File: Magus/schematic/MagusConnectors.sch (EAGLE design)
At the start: 48 parts, among them IC3 RC4560, J1 POWER_JACK, U1 REG_S9V11F5, U2 REG_U3V12F12, U3 ICL7660, X2 1503_09, X4 1503_09, X5 1503_09

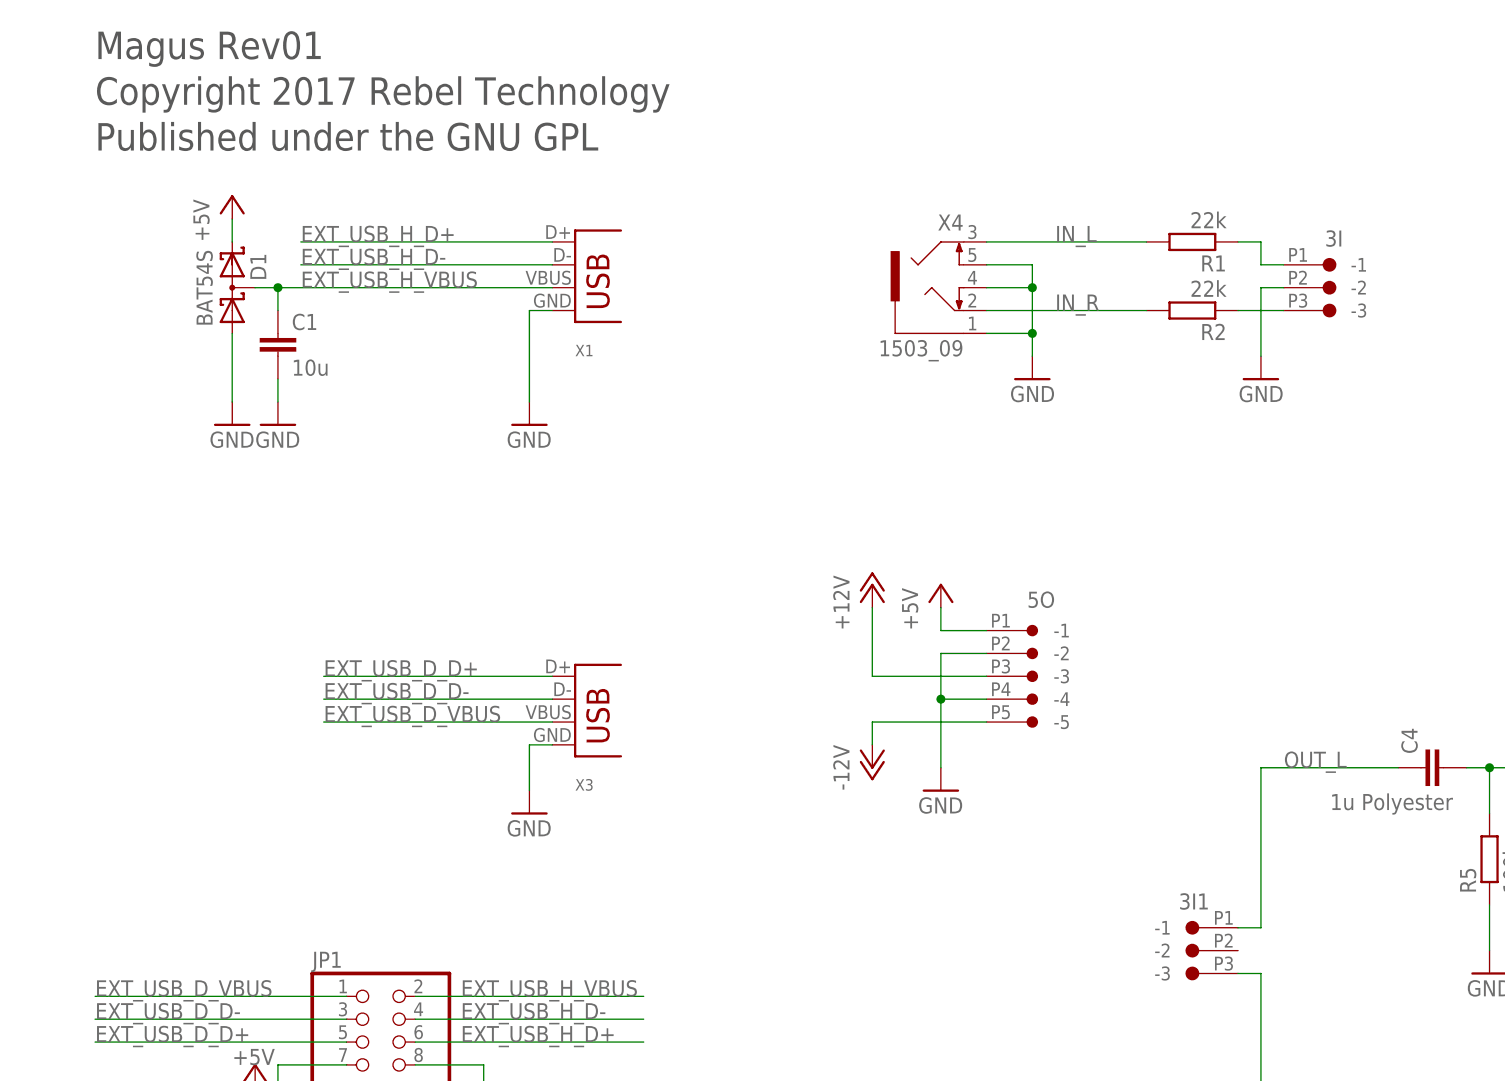
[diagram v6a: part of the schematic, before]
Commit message: moved BUS1 (uart)
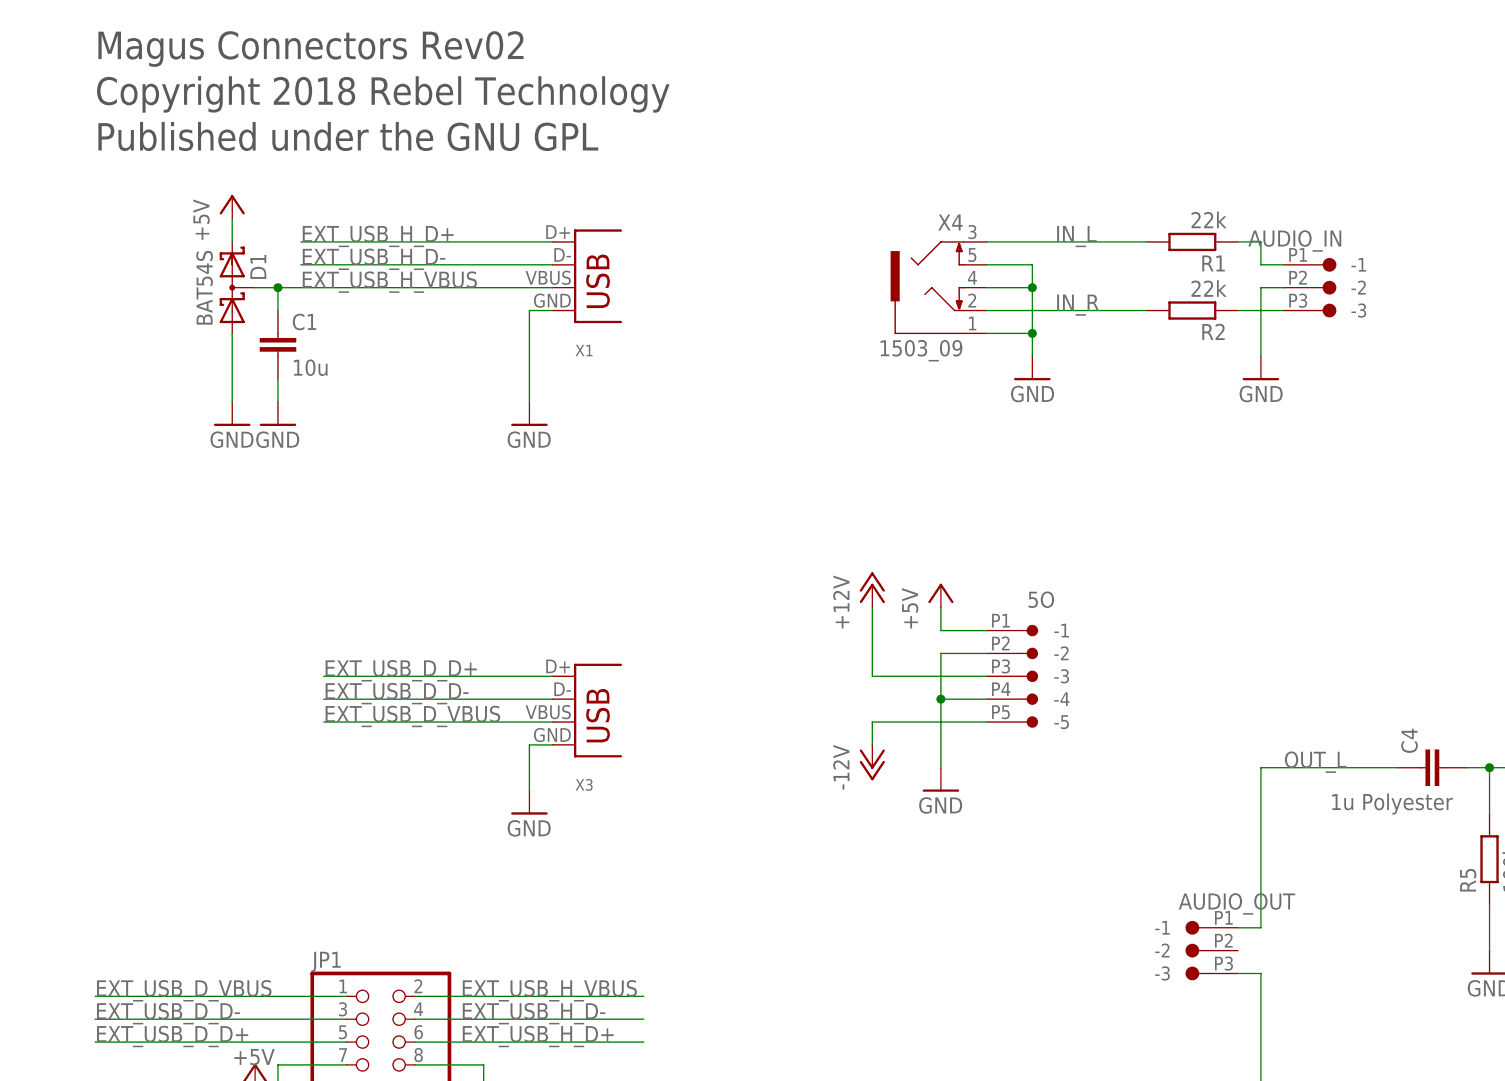
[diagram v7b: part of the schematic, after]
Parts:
- renumbered 3I to AUDIO_IN, 3I1 to AUDIO_OUT
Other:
- note added: "Copyright 2018 Rebel Technology"
- note added: "Magus Connectors Rev02"
- note removed: "Copyright 2017 Rebel Technology"
- note removed: "Magus Rev01"
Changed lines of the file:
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@@
 <part name="GND23" library="supply1" deviceset="GND" device=""/>
 <part name="5O" library="Rebel" deviceset="CON-JST_PH_5W" device=""/>
-<part name="3I" library="Rebel" deviceset="CON-JST_PH_3W" device=""/>
+<part name="AUDIO_IN" library="Rebel" deviceset="CON-JST_PH_3W" device=""/>
 <part name="R1" library="resistor" deviceset="R-EU_" device="R0603" value="22k"/>
 <part name="R2" library="resistor" deviceset="R-EU_" device="R0603" value="22k"/>
@@
 <part name="P+4" library="supply1" deviceset="+12V" device=""/>
 <part name="P-1" library="supply1" deviceset="-12V" device=""/>
-<part name="3I1" library="Rebel" deviceset="CON-JST_PH_3W" device=""/>
+<part name="AUDIO_OUT" library="Rebel" deviceset="CON-JST_PH_3W" device=""/>
 <part name="C6" library="rcl" deviceset="C-EU" device="C0603" value="100n"/>
 <part name="GND4" library="supply1" deviceset="GND" device=""/>
@@
 <sheet>
 <plain>
-<text x="5.08" y="119.38" size="3.048" layer="97" font="vector">Magus Rev01</text>
-<text x="5.08" y="114.3" size="3.048" layer="97" font="vector">Copyright 2017 Rebel Technology</text>
+<text x="5.08" y="119.38" size="3.048" layer="97" font="vector">Magus Connectors Rev02</text>
+<text x="5.08" y="114.3" size="3.048" layer="97" font="vector">Copyright 2018 Rebel Technology</text>
 <text x="5.08" y="109.22" size="3.048" layer="97" font="vector">Published under the GNU GPL</text>
 </plain>
@@
 <instance part="GND23" gate="1" x="177.8" y="-22.86"/>
 <instance part="5O" gate="G$1" x="109.22" y="55.88" rot="MR0"/>
-<instance part="3I" gate="G$1" x="137.16" y="96.52" rot="MR0"/>
+<instance part="AUDIO_IN" gate="G$1" x="137.16" y="96.52" rot="MR0"/>
 <instance part="R1" gate="G$1" x="127" y="99.06" rot="R180"/>
 <instance part="R2" gate="G$1" x="127" y="91.44" rot="R180"/>
@@
 <instance part="P+4" gate="1" x="91.44" y="60.96"/>
 <instance part="P-1" gate="1" x="91.44" y="40.64"/>
-<instance part="3I1" gate="G$1" x="132.08" y="22.86"/>
+<instance part="AUDIO_OUT" gate="G$1" x="132.08" y="22.86"/>
 <instance part="C6" gate="G$1" x="5.08" y="-43.18" rot="R180"/>
 <instance part="GND4" gate="1" x="22.86" y="-53.34"/>
@@
 </segment>
 <segment>
-<pinref part="3I" gate="G$1" pin="-2"/>
+<pinref part="AUDIO_IN" gate="G$1" pin="-2"/>
 <pinref part="GND2" gate="1" pin="GND"/>
 <wire x1="137.16" y1="93.98" x2="134.62" y2="93.98" width="0.1524" layer="91"/>
@@
 <wire x1="134.62" y1="40.64" x2="149.86" y2="40.64" width="0.1524" layer="91"/>
 <label x="137.16" y="40.64" size="1.778" layer="95"/>
-<pinref part="3I1" gate="G$1" pin="-1"/>
+<pinref part="AUDIO_OUT" gate="G$1" pin="-1"/>
 <wire x1="132.08" y1="22.86" x2="134.62" y2="22.86" width="0.1524" layer="91"/>
 <wire x1="134.62" y1="22.86" x2="134.62" y2="40.64" width="0.1524" layer="91"/>
@@
 <pinref part="C5" gate="G$1" pin="1"/>
 <label x="137.16" y="0" size="1.778" layer="95"/>
-<pinref part="3I1" gate="G$1" pin="-3"/>
+<pinref part="AUDIO_OUT" gate="G$1" pin="-3"/>
 <wire x1="132.08" y1="17.78" x2="134.62" y2="17.78" width="0.1524" layer="91"/>
 <wire x1="134.62" y1="17.78" x2="134.62" y2="0" width="0.1524" layer="91"/>
@@
 <segment>
 <pinref part="R2" gate="G$1" pin="1"/>
-<pinref part="3I" gate="G$1" pin="-3"/>
+<pinref part="AUDIO_IN" gate="G$1" pin="-3"/>
 <wire x1="132.08" y1="91.44" x2="137.16" y2="91.44" width="0.1524" layer="91"/>
 </segment>
@@
 <net name="N$6" class="0">
 <segment>
-<pinref part="3I" gate="G$1" pin="-1"/>
+<pinref part="AUDIO_IN" gate="G$1" pin="-1"/>
 <wire x1="137.16" y1="96.52" x2="134.62" y2="96.52" width="0.1524" layer="91"/>
 <wire x1="134.62" y1="96.52" x2="134.62" y2="99.06" width="0.1524" layer="91"/>

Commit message: updated part values
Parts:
- C15, C3: value 680p -> 750p
- U1: value REG_S9V11F5 -> S9V11F5
- U2: value REG_U3V12F12 -> S10V2F12
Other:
- note added: "LPF 21kHz"
- moved on the sheet: C15, C3
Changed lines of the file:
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@@
 <part name="GND7" library="supply1" deviceset="GND" device=""/>
 <part name="SUPPLY3" library="supply2" deviceset="+9V" device=""/>
-<part name="U1" library="Rebel" deviceset="REG_S9V11F5" device=""/>
-<part name="U2" library="Rebel" deviceset="REG_S9V11F5" device="" value="REG_U3V12F12"/>
+<part name="U1" library="Rebel" deviceset="REG_S9V11F5" device="" value="S9V11F5"/>
+<part name="U2" library="Rebel" deviceset="REG_S9V11F5" device="" value="S10V2F12"/>
 <part name="C12" library="rcl" deviceset="C-EU" device="C0603" value="100n"/>
 <part name="GND11" library="supply1" deviceset="GND" device=""/>
@@
 <part name="C2" library="Rebel" deviceset="CPOL-EU" device="D" value="2200u 10v"/>
 <part name="GND15" library="supply1" deviceset="GND" device=""/>
-<part name="C3" library="Rebel" deviceset="C-EU" device="C0603" value="680p"/>
-<part name="C15" library="Rebel" deviceset="C-EU" device="C0603" value="680p"/>
+<part name="C3" library="Rebel" deviceset="C-EU" device="C0603" value="750p"/>
+<part name="C15" library="Rebel" deviceset="C-EU" device="C0603" value="750p"/>
 <part name="X5" library="con-lumberg" deviceset="1503_09" device=""/>
 <part name="EXT" library="Rebel" deviceset="CON-JST_PH_3W" device=""/>
@@
 <text x="5.08" y="114.3" size="3.048" layer="97" font="vector">Copyright 2018 Rebel Technology</text>
 <text x="5.08" y="109.22" size="3.048" layer="97" font="vector">Published under the GNU GPL</text>
+<text x="200.66" y="12.7" size="1.778" layer="97">LPF 21kHz</text>
 </plain>
 <instances>
@@
 </instance>
 <instance part="GND15" gate="1" x="124.46" y="-50.8"/>
-<instance part="C3" gate="G$1" x="195.58" y="22.86" smashed="yes" rot="R270">
-<attribute name="NAME" x="195.961" y="21.336" size="1.778" layer="95" rot="R270"/>
-<attribute name="VALUE" x="192.024" y="25.781" size="1.778" layer="96"/>
-</instance>
-<instance part="C15" gate="G$1" x="198.12" y="-17.78" smashed="yes" rot="R270">
-<attribute name="NAME" x="198.501" y="-19.304" size="1.778" layer="95" rot="R270"/>
-<attribute name="VALUE" x="194.564" y="-14.859" size="1.778" layer="96"/>
+<instance part="C3" gate="G$1" x="195.58" y="20.32" smashed="yes" rot="R270">
+<attribute name="NAME" x="195.961" y="18.796" size="1.778" layer="95" rot="R270"/>
+<attribute name="VALUE" x="192.024" y="23.241" size="1.778" layer="96"/>
+</instance>
+<instance part="C15" gate="G$1" x="198.12" y="-20.32" smashed="yes" rot="R270">
+<attribute name="NAME" x="198.501" y="-21.844" size="1.778" layer="95" rot="R270"/>
+<attribute name="VALUE" x="194.564" y="-17.399" size="1.778" layer="96"/>
 </instance>
 <instance part="X5" gate="G$1" x="172.72" y="96.52" rot="MR0"/>
@@
 <junction x="205.74" y="43.18"/>
 <pinref part="C3" gate="G$1" pin="1"/>
-<wire x1="198.12" y1="22.86" x2="205.74" y2="22.86" width="0.1524" layer="91"/>
-<wire x1="205.74" y1="22.86" x2="205.74" y2="30.48" width="0.1524" layer="91"/>
+<wire x1="198.12" y1="20.32" x2="205.74" y2="20.32" width="0.1524" layer="91"/>
+<wire x1="205.74" y1="20.32" x2="205.74" y2="30.48" width="0.1524" layer="91"/>
 <junction x="205.74" y="30.48"/>
 </segment>
@@
 <junction x="205.74" y="2.54"/>
 <pinref part="C15" gate="G$1" pin="1"/>
-<wire x1="200.66" y1="-17.78" x2="205.74" y2="-17.78" width="0.1524" layer="91"/>
-<wire x1="205.74" y1="-17.78" x2="205.74" y2="-10.16" width="0.1524" layer="91"/>
+<wire x1="200.66" y1="-20.32" x2="205.74" y2="-20.32" width="0.1524" layer="91"/>
+<wire x1="205.74" y1="-20.32" x2="205.74" y2="-10.16" width="0.1524" layer="91"/>
 <junction x="205.74" y="-10.16"/>
 </segment>
@@
 <junction x="185.42" y="40.64"/>
 <pinref part="C3" gate="G$1" pin="2"/>
-<wire x1="190.5" y1="22.86" x2="185.42" y2="22.86" width="0.1524" layer="91"/>
-<wire x1="185.42" y1="22.86" x2="185.42" y2="30.48" width="0.1524" layer="91"/>
+<wire x1="190.5" y1="20.32" x2="185.42" y2="20.32" width="0.1524" layer="91"/>
+<wire x1="185.42" y1="20.32" x2="185.42" y2="30.48" width="0.1524" layer="91"/>
 <junction x="185.42" y="30.48"/>
 </segment>
@@
 <junction x="185.42" y="0"/>
 <pinref part="C15" gate="G$1" pin="2"/>
-<wire x1="193.04" y1="-17.78" x2="185.42" y2="-17.78" width="0.1524" layer="91"/>
-<wire x1="185.42" y1="-17.78" x2="185.42" y2="-10.16" width="0.1524" layer="91"/>
+<wire x1="193.04" y1="-20.32" x2="185.42" y2="-20.32" width="0.1524" layer="91"/>
+<wire x1="185.42" y1="-20.32" x2="185.42" y2="-10.16" width="0.1524" layer="91"/>
 <junction x="185.42" y="-10.16"/>
 </segment>
